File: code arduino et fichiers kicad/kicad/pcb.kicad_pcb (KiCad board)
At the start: 4 copper layers, 53.3 x 101.6 mm, 29 parts, among them U1 LMC6482, U2 LMC6482, U3 LMC6482

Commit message: kasjd
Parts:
- added J1: Screw_Terminal_01x04, Connector_JST:JST_XH_B4B-XH-A_1x04_P2.50mm_Vertical, F.Cu at (85.2, 108.5)
- added J2: Screw_Terminal_01x04, Connector_JST:JST_XH_B4B-XH-A_1x04_P2.50mm_Vertical, F.Cu at (97.7, 108.4)
- added J3: Screw_Terminal_01x02, Connector_JST:JST_XH_B2B-XH-A_1x02_P2.50mm_Vertical, F.Cu at (109.6, 113.5)
- TH1, TH2, TH3: footprint TerminalBlock_Phoenix:TerminalBlock_Phoenix_MPT-0,5-2-2.54_1x02_P2.54mm_Horizontal -> Connector_JST:JST_XH_B2B-XH-A_1x02_P2.50mm_Vertical
- moved R5 28.7 mm to (79.8, 56.2)
- moved R11 27.4 mm to (84.0, 68.3)
- moved R15 26.7 mm to (90.1, 85.4)
- moved R7 20.8 mm to (96.3, 59.2)
- moved R1 20.3 mm to (79.6, 51.5)
- moved R2 20.0 mm to (79.8, 61.2)
- moved U2 16.9 mm to (97.9, 71.7)
- moved R10 16.3 mm to (89.7, 68.1)
- moved U1 15.9 mm to (88.4, 56.9)
- moved TH3 15.7 mm to (116.4, 43.0), turned to 0 degrees
- moved R9 15.2 mm to (89.7, 71.6)
- moved R3 14.6 mm to (96.1, 53.8)
- moved R14 14.5 mm to (84.8, 96.1)
- moved R13 14.3 mm to (90.6, 96.2)
- moved U3 14.2 mm to (98.3, 89.1)
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
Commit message: procrastination pendant optique
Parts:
- removed J3: Screw_Terminal_01x02, Connector_JST:JST_XH_B2B-XH-A_1x02_P2.50mm_Vertical
- added LED1: LED_LEDCHIP-LED0805, LED_SMD:LED_0805_2012Metric_Pad1.15x1.40mm_HandSolder, F.Cu at (78.9, 57.8)
- added R18: 560, Resistor_SMD:R_0805_2012Metric_Pad1.20x1.40mm_HandSolder, F.Cu at (75.1, 57.8)
- moved J1 42.4 mm to (110.0, 74.2)
- moved R11 36.8 mm to (99.1, 101.9), turned to -90 degrees
- moved R12 31.2 mm to (99.1, 106.2), turned to 90 degrees
- moved R7 28.7 mm to (99.3, 87.7), turned to 90 degrees
- moved R6 24.5 mm to (99.3, 83.4), turned to -90 degrees
- moved R8 21.7 mm to (85.0, 83.5), turned to -90 degrees
- moved J2 21.5 mm to (110.2, 91.0)
- moved R10 20.4 mm to (85.0, 87.9), turned to 90 degrees
- moved R15 17.3 mm to (84.9, 101.9), turned to 90 degrees
- moved U3 17.2 mm to (92.0, 105.1)
- moved U2 16.1 mm to (91.9, 86.6)
- moved R4 15.0 mm to (99.3, 68.7), turned to -90 degrees
- moved R1 13.9 mm to (84.9, 64.3), turned to 90 degrees
- moved R5 12.6 mm to (92.1, 59.0), turned to 180 degrees
- moved R13 11.5 mm to (85.0, 106.3), turned to 90 degrees
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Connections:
- power2 pad 4: unconnected-(power2-Pin_4-Pad4) -> +3.3V
- power2 pad 5: unconnected-(power2-Pin_5-Pad5) -> 5V
- power2 pad 7: unconnected-(power2-Pin_7-Pad7) -> GND
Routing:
- net +5V: track 0.00 -> 104.6 mm
- net Net-(U3A--): track 0.00 -> 75.3 mm
- net Net-(U2A--): track 0.00 -> 54.0 mm, vias 0 -> 1
- net T1 sortie: track 0.00 -> 37.3 mm
- net Net-(U1A--): track 0.00 -> 31.7 mm
- net T2 sortie: track 0.00 -> 25.5 mm
- net T3 sortie: track 0.00 -> 18.5 mm
- net Net-(U1B-+): track 0.00 -> 18.3 mm
- net Net-(U2B-+): track 0.00 -> 18.2 mm
- net +3.3V: track 0.00 -> 17.9 mm
- net Net-(U3B-+): track 0.00 -> 17.4 mm
- net pwmgauche: track 0.00 -> 9.46 mm
- net pwmdroite: track 0.00 -> 9.24 mm
- net Net-(U1B--): track 0.00 -> 8.78 mm
- net Net-(U2A-+): track 0.00 -> 8.54 mm
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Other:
- outline, holes or cut-outs redrawn
- board text added: "R14"
- board text added: "analog in"
- board text added: "communication"
- board text added: "digital"
- board text added: "power"
- board text added: "pwm"

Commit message: ksjkasjdh
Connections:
- analogA0-A7 pad 4: unconnected-(analogA0-A7-Pin_4-Pad4) -> /A3
- analogA0-A7 pad 5: unconnected-(analogA0-A7-Pin_5-Pad5) -> /A4
- analogA0-A7 pad 6: unconnected-(analogA0-A7-Pin_6-Pad6) -> /A5
- analogA0-A7 pad 7: unconnected-(analogA0-A7-Pin_7-Pad7) -> /A6
- analogA0-A7 pad 8: unconnected-(analogA0-A7-Pin_8-Pad8) -> /A7
- analogA8-A15 pad 1: unconnected-(analogA8-A15-Pin_1-Pad1) -> /A8
- analogA8-A15 pad 2: unconnected-(analogA8-A15-Pin_2-Pad2) -> /A9
- analogA8-A15 pad 3: unconnected-(analogA8-A15-Pin_3-Pad3) -> /A10
- analogA8-A15 pad 4: unconnected-(analogA8-A15-Pin_4-Pad4) -> /A11
- analogA8-A15 pad 5: unconnected-(analogA8-A15-Pin_5-Pad5) -> /A12
- analogA8-A15 pad 6: unconnected-(analogA8-A15-Pin_6-Pad6) -> /A13
- analogA8-A15 pad 7: unconnected-(analogA8-A15-Pin_7-Pad7) -> /A14
- analogA8-A15 pad 8: unconnected-(analogA8-A15-Pin_8-Pad8) -> /A15
- comm1 pad 1: unconnected-(comm1-Pin_1-Pad1) -> /D14
- comm1 pad 2: unconnected-(comm1-Pin_2-Pad2) -> /D15
- comm1 pad 3: unconnected-(comm1-Pin_3-Pad3) -> /D16
- comm1 pad 4: unconnected-(comm1-Pin_4-Pad4) -> /D17
- comm1 pad 5: unconnected-(comm1-Pin_5-Pad5) -> /D18
- comm1 pad 6: unconnected-(comm1-Pin_6-Pad6) -> /D19
- comm1 pad 7: unconnected-(comm1-Pin_7-Pad7) -> /D20
- comm1 pad 8: unconnected-(comm1-Pin_8-Pad8) -> /D21
- digital1 pad 1: unconnected-(digital1-Pin_1-Pad1) -> +5V
- digital1 pad 18: unconnected-(digital1-Pin_18-Pad18) -> GND
- digital2 pad 1: unconnected-(digital2-Pin_1-Pad1) -> +5V
- digital2 pad 18: unconnected-(digital2-Pin_18-Pad18) -> GND
- power2 pad 2: unconnected-(power2-Pin_2-Pad2) -> +IOREF
- power2 pad 3: unconnected-(power2-Pin_3-Pad3) -> /RESET
- power2 pad 5: 5V -> +5V
- power2 pad 8: unconnected-(power2-Pin_8-Pad8) -> +VIN
- pwm1 pad 1: unconnected-(pwm1-Pin_1-Pad1) -> /D8
- pwm1 pad 10: unconnected-(pwm1-Pin_10-Pad10) -> /SCL
- pwm1 pad 2: unconnected-(pwm1-Pin_2-Pad2) -> /D9
- pwm1 pad 3: unconnected-(pwm1-Pin_3-Pad3) -> /D10
- pwm1 pad 4: unconnected-(pwm1-Pin_4-Pad4) -> pwmgauche
- pwm1 pad 5: unconnected-(pwm1-Pin_5-Pad5) -> /D12
- pwm1 pad 6: unconnected-(pwm1-Pin_6-Pad6) -> /D13
- pwm1 pad 7: pwmgauche -> GND
- pwm1 pad 8: unconnected-(pwm1-Pin_8-Pad8) -> +AREF
- pwm1 pad 9: unconnected-(pwm1-Pin_9-Pad9) -> /SDA
- pwm2 pad 1: unconnected-(pwm2-Pin_1-Pad1) -> /D0/RX0
- pwm2 pad 2: unconnected-(pwm2-Pin_2-Pad2) -> /D1/TX0
- pwm2 pad 3: pwmdroite -> /D2
- pwm2 pad 4: unconnected-(pwm2-Pin_4-Pad4) -> /D3
- pwm2 pad 5: unconnected-(pwm2-Pin_5-Pad5) -> /D4
- pwm2 pad 6: unconnected-(pwm2-Pin_6-Pad6) -> pwmdroite
- pwm2 pad 7: unconnected-(pwm2-Pin_7-Pad7) -> /D6
- pwm2 pad 8: unconnected-(pwm2-Pin_8-Pad8) -> /D7
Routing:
- net +5V: track 104.6 -> 181.4 mm
- net pwmgauche: track 9.46 -> 12.6 mm
- net pwmdroite: track 9.24 -> 12.2 mm

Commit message: pcb yaddi yadda
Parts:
- removed LED1: LED_LEDCHIP-LED0805, LED_SMD:LED_0805_2012Metric_Pad1.15x1.40mm_HandSolder
- added D4: LED, PCM_SparkFun-LED:LED_0603_1608Metric, F.Cu at (79.6, 57.6)
- added TP1: TestPoint, TestPoint:TestPoint_THTPad_D1.5mm_Drill0.7mm, F.Cu at (86.5, 58.8)
- added TP2: TestPoint, TestPoint:TestPoint_THTPad_D1.5mm_Drill0.7mm, F.Cu at (86.0, 78.2)
- added TP3: TestPoint, TestPoint:TestPoint_THTPad_D1.5mm_Drill0.7mm, F.Cu at (86.4, 96.8)
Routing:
- net Net-(U2A--): track 54.0 -> 43.5 mm, vias 1 -> 0
- net +5V: track 181.4 -> 191.1 mm, vias 0 -> 1
- net T2 sortie: track 25.5 -> 33.6 mm
- net Net-(U1A--): track 31.7 -> 25.3 mm
- net T1 sortie: track 37.3 -> 43.5 mm
- net Net-(U3A--): track 75.3 -> 70.0 mm, vias 0 -> 1
- net Net-(D4-A): track 0.00 -> 4.51 mm
- net T3 sortie: track 18.5 -> 22.3 mm
- net (no net): track 2.91 -> 0.00 mm
- net Net-(U3B-+): track 17.4 -> 16.0 mm, vias 0 -> 1
- net Net-(U2A-+): track 8.54 -> 7.17 mm
- net Net-(U1B--): track 8.78 -> 7.48 mm
- net Net-(U3B--): track 5.91 -> 6.76 mm
- net Net-(U1B-+): track 18.3 -> 17.6 mm, vias 0 -> 1
- net Net-(U2B-+): track 18.2 -> 17.8 mm, vias 0 -> 1
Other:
- copper layers 4 -> 2

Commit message: version tht pour pas trop haïr notre vie plus tard
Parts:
- removed J2: Screw_Terminal_01x04, Connector_JST:JST_XH_B4B-XH-A_1x04_P2.50mm_Vertical
- removed R1, R10, R15: 6.1K, Resistor_SMD:R_0805_2012Metric_Pad1.20x1.40mm_HandSolder
- removed digital1, digital2: Conn_01x18_Pin, Connector_PinHeader_2.54mm:PinHeader_1x18_P2.54mm_Vertical
- added C16: 2 μF, Capacitor_THT:CP_Radial_D5.0mm_P2.50mm, F.Cu at (81.9, 59.9)
- added C17: 2 μF, Capacitor_THT:CP_Radial_D5.0mm_P2.50mm, F.Cu at (82.6, 82.8)
- added C18: 2 μF, Capacitor_THT:CP_Radial_D5.0mm_P2.50mm, F.Cu at (82.0, 105.4)
- added J3: Screw_Terminal_01x02, Connector_JST:JST_XH_B2B-XH-A_1x02_P2.50mm_Vertical, F.Cu at (77.0, 45.7)
- added RV1: R_Potentiometer_Trim, Library:trimpot, F.Cu at (76.0, 70.0)
- added RV2: R_Potentiometer_Trim, Library:trimpot, F.Cu at (76.2, 93.0)
- added RV3: R_Potentiometer_Trim, Library:trimpot, F.Cu at (91.2, 117.1)
- D4: footprint PCM_SparkFun-LED:LED_0603_1608Metric -> LED_THT:LED_D5.0mm
- R11, R12, R13, R14, R18, R2, R3, R4, R5, R6, R7, R8, R9: footprint Resistor_SMD:R_0805_2012Metric_Pad1.20x1.40mm_HandSolder -> Resistor_THT:R_Axial_DIN0207_L6.3mm_D2.5mm_P7.62mm_Horizontal
- moved TH3 87.2 mm to (109.2, 132.1), turned to 180 degrees
- moved TH2 86.9 mm to (96.9, 131.8), turned to 180 degrees
- moved TH1 86.6 mm to (85.5, 131.6), turned to 180 degrees
- moved R18 74.6 mm to (77.2, 132.4)
- moved D4 63.6 mm to (77.0, 121.2)
- moved J1 28.4 mm to (108.0, 45.8), turned to 0 degrees
- moved R11 20.4 mm to (106.0, 121.1), turned to 90 degrees
- moved R12 18.9 mm to (110.8, 121.0)
- moved R13 15.2 mm to (89.9, 120.7)
- moved R3 13.4 mm to (112.6, 65.8)
- moved U3 13.3 mm to (97.9, 117.1)
- moved R7 12.9 mm to (112.2, 88.7), turned to -90 degrees
- moved R9 12.1 mm to (102.2, 84.5)
- moved TP3 10.7 mm to (89.6, 107.0)
- moved R5 10.2 mm to (102.1, 60.7)
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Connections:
- J1 pad 3: unconnected-(J1-Pin_3-Pad3) -> pwmdroite
- R18 pad 1: +3.3V -> +5V
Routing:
- net Net-(U1A--): track 25.3 -> 75.1 mm
- net pwmdroite: track 12.2 -> 57.1 mm
- net +5V: track 191.1 -> 162.7 mm, vias 1 -> 0
- net Net-(U3A--): track 70.0 -> 44.3 mm, vias 1 -> 0
- net T3 sortie: track 22.3 -> 46.3 mm
- net Net-(U1A-+): track 6.07 -> 28.2 mm
- net Net-(U2A-+): track 7.17 -> 26.7 mm
- net +3.3V: track 17.9 -> 0.00 mm
- net Net-(U3A-+): track 5.91 -> 23.7 mm
- net pwmgauche: track 12.6 -> 30.1 mm
- net T1 sortie: track 43.5 -> 50.3 mm
- net T2 sortie: track 33.6 -> 39.3 mm
- net Net-(U2A--): track 43.5 -> 48.9 mm
- net Net-(U2B--): track 6.20 -> 10.9 mm
- net Net-(U3B--): track 6.76 -> 11.4 mm
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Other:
- board text removed: "digital"

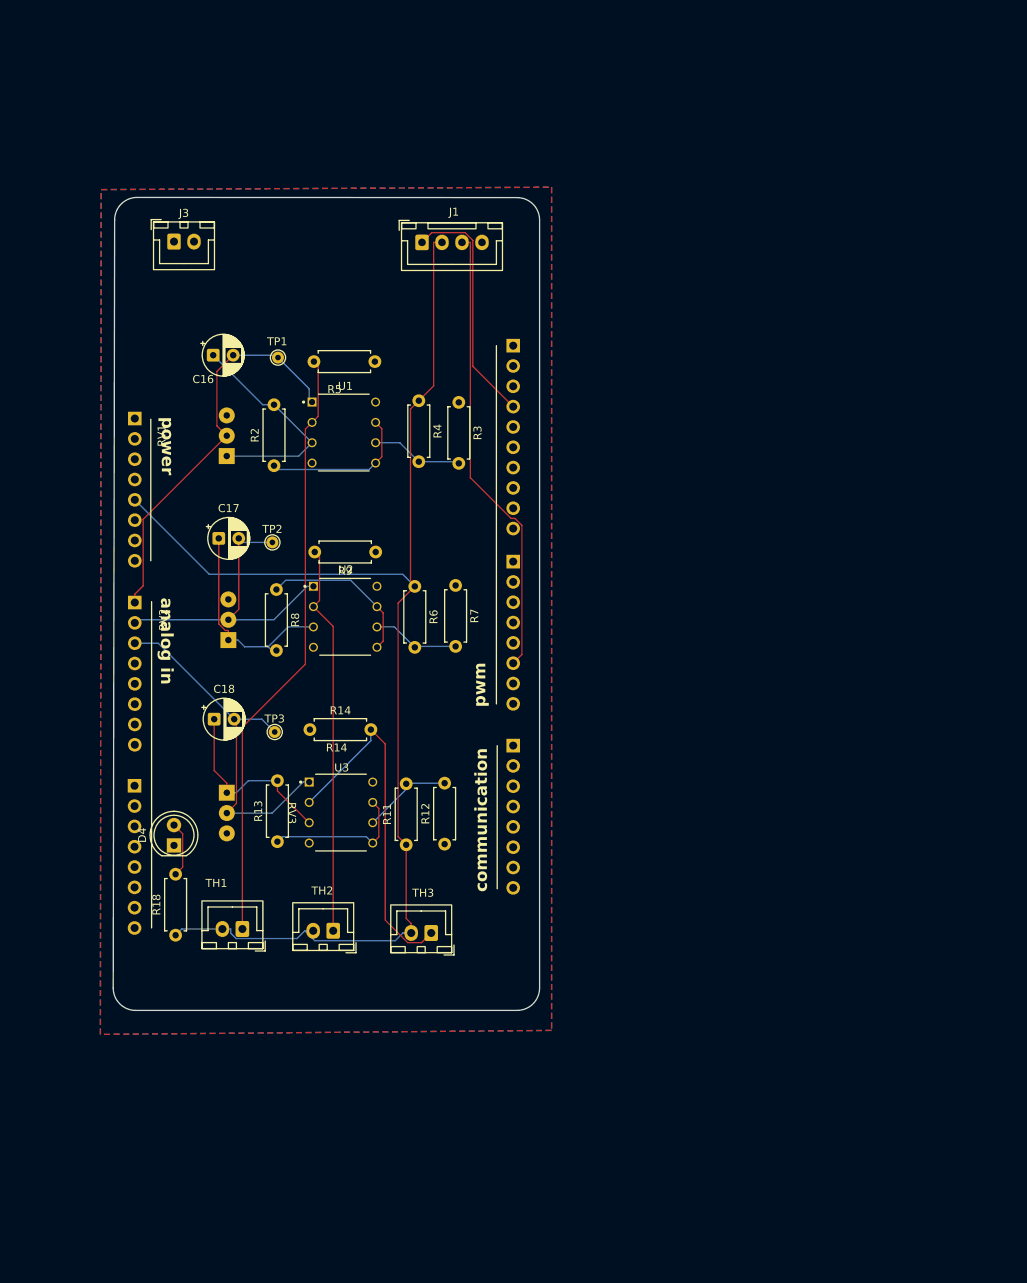
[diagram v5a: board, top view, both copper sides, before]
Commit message: Changment connecteur pcb
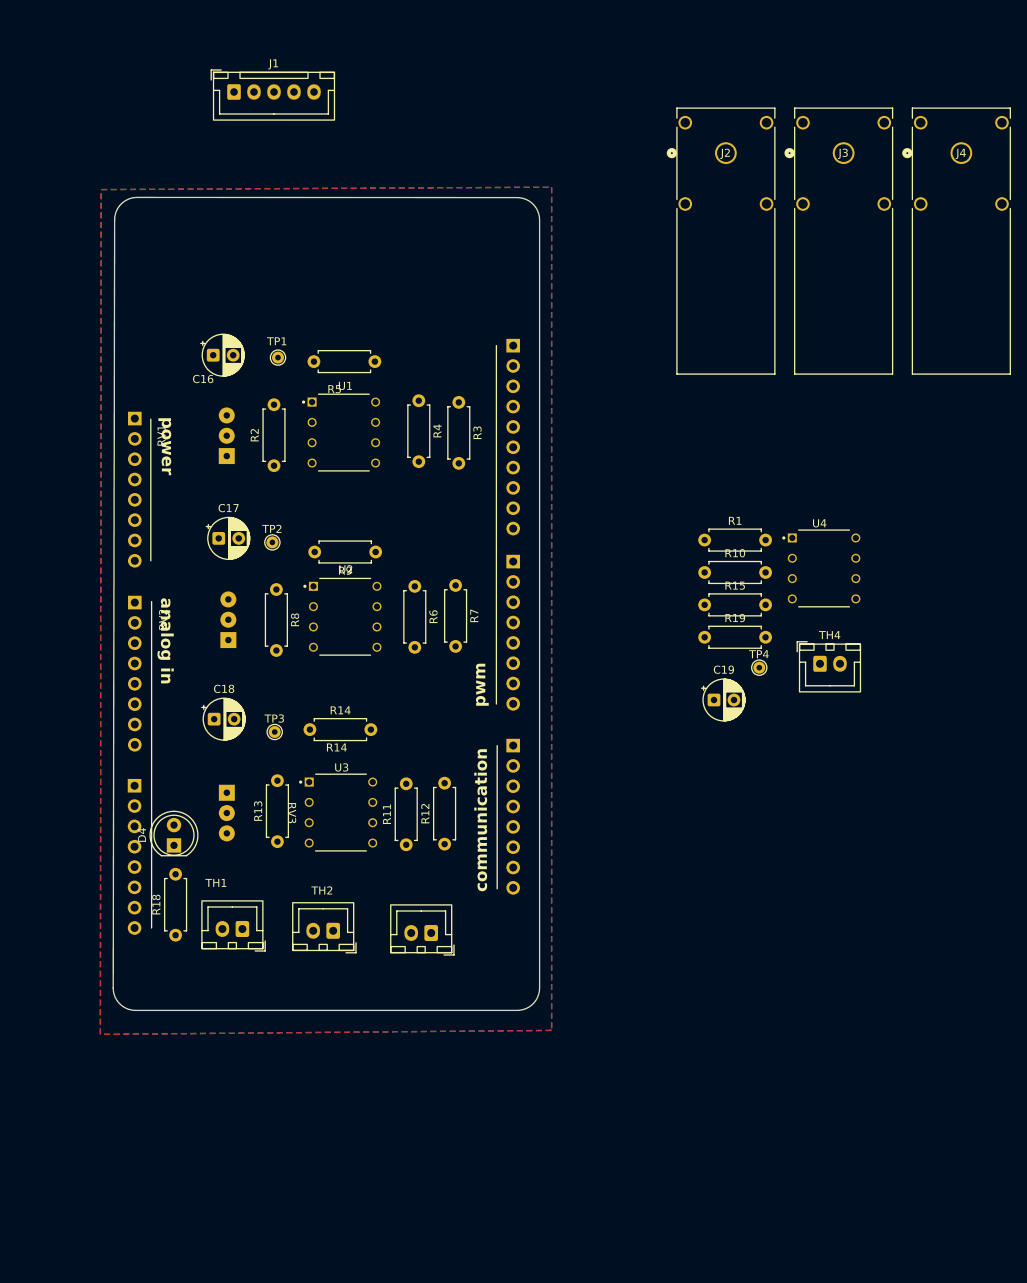
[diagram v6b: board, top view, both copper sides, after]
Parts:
- added C19: 2 μF, Capacitor_THT:CP_Radial_D5.0mm_P2.50mm, F.Cu at (144.5, 103.0)
- added J2: FCR7350R, Connector:CONN1_FCR7350R_CLF, F.Cu at (146.0, 34.6)
- added J4: FCR7350R, Connector:CONN1_FCR7350R_CLF, F.Cu at (175.4, 34.6)
- added R1: 10K, Resistor_THT:R_Axial_DIN0207_L6.3mm_D2.5mm_P7.62mm_Horizontal, F.Cu at (143.3, 83.0)
- added R10: 6.1K, Resistor_THT:R_Axial_DIN0207_L6.3mm_D2.5mm_P7.62mm_Horizontal, F.Cu at (143.3, 87.1)
- added R15: 2K, Resistor_THT:R_Axial_DIN0207_L6.3mm_D2.5mm_P7.62mm_Horizontal, F.Cu at (143.3, 91.1)
- added R19: 6.1K, Resistor_THT:R_Axial_DIN0207_L6.3mm_D2.5mm_P7.62mm_Horizontal, F.Cu at (143.3, 95.2)
- added TH4: Thermistor, Connector_JST:JST_XH_B2B-XH-A_1x02_P2.50mm_Vertical, F.Cu at (157.8, 98.5)
- added TP4: TestPoint, TestPoint:TestPoint_THTPad_D1.5mm_Drill0.7mm, F.Cu at (150.2, 99.0)
- added U4: LMC6482, ampli op:LMC6482, F.Cu at (159.7, 87.8)
- J1: value Screw_Terminal_01x04 -> Screw_Terminal_01x05; footprint Connector_JST:JST_XH_B4B-XH-A_1x04_P2.50mm_Vertical -> Connector_JST:JST_XH_B5B-XH-A_1x05_P2.50mm_Vertical
- J3: value Screw_Terminal_01x02 -> FCR7350R; footprint Connector_JST:JST_XH_B2B-XH-A_1x02_P2.50mm_Vertical -> Connector:CONN1_FCR7350R_CLF
- moved J3 84.4 mm to (160.7, 34.6)
- moved J1 30.1 mm to (84.5, 27.0)
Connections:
- J1 pad 2: +5V -> pwmdroite
- J1 pad 3: pwmdroite -> +8V
- J1 pad 4: GND -> +5V
- J3 pad 1: GND -> +5V
- J3 pad 2: +8V -> (no net)
- analogA0-A7 pad 4: /A3 -> T4 sortie
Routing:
- net +5V: track 162.7 -> 0.00 mm
- net Net-(U1A--): track 75.1 -> 0.75 mm
- net pwmdroite: track 57.1 -> 0.00 mm
- net T1 sortie: track 50.3 -> 0.42 mm
- net Net-(U2A--): track 48.9 -> 0.00 mm
- net T3 sortie: track 46.3 -> 0.40 mm
- net Net-(U3A--): track 44.3 -> 0.00 mm
- net T2 sortie: track 39.3 -> 0.00 mm
- net pwmgauche: track 30.1 -> 0.00 mm
- net Net-(U1A-+): track 28.2 -> 0.01 mm
- net Net-(U2A-+): track 26.7 -> 0.00 mm
- net Net-(U3A-+): track 23.7 -> 0.00 mm
- net Net-(U2B-+): track 20.1 -> 0.00 mm
- net Net-(U1B-+): track 19.0 -> 0.00 mm
- net Net-(U3B-+): track 18.2 -> 0.00 mm
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
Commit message: Pcb quasi fini
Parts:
- added RV4: R_Potentiometer_Trim, Library:trimpot, F.Cu at (102.0, 104.4)
- C16, C17, C18, C19: footprint Capacitor_THT:CP_Radial_D5.0mm_P2.50mm -> Library:condensateur 1uF
- R1, R10, R11, R12, R13, R14, R15, R18, R19, R2, R3, R4, R5, R6, R7, R8, R9: footprint Resistor_THT:R_Axial_DIN0207_L6.3mm_D2.5mm_P7.62mm_Horizontal -> Library:Resistance SMT
- moved J4 92.1 mm to (84.5, 49.5), turned to 180 degrees
- moved R18 71.6 mm to (90.0, 62.0), turned to -90 degrees
- moved U4 66.6 mm to (103.5, 123.5)
- moved J3 63.3 mm to (99.2, 49.5), turned to 180 degrees
- moved D4 60.9 mm to (96.0, 63.3)
- moved TH4 59.4 mm to (112.5, 137.0), turned to 180 degrees
- moved R1 54.1 mm to (111.3, 126.7), turned to 180 degrees
- moved R10 48.6 mm to (111.4, 123.7), turned to 180 degrees
- moved R15 43.6 mm to (111.3, 120.7), turned to 180 degrees
- moved C19 42.0 mm to (102.5, 102.0)
- moved TP4 41.3 mm to (111.0, 112.0)
- moved R19 39.1 mm to (111.3, 117.7), turned to 180 degrees
- moved J2 35.3 mm to (113.9, 49.5), turned to 180 degrees
- moved RV2 34.2 mm to (103.5, 72.4), turned to 0 degrees
- moved R3 32.2 mm to (93.5, 91.7), turned to 180 degrees
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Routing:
- net GND: track 0.00 -> 170.4 mm
- net pwmdroite: track 0.00 -> 97.3 mm
- net Net-(U2A--): track 0.00 -> 95.8 mm
- net Net-(U1A--): track 0.75 -> 76.7 mm
- net T2 sortie: track 0.00 -> 66.5 mm
- net T4 sortie: track 0.00 -> 64.1 mm
- net pwmgauche: track 0.00 -> 59.2 mm
- net +8V: track 0.00 -> 57.9 mm
- net Net-(U1A-+): track 0.01 -> 51.9 mm
- net T3 sortie: track 0.40 -> 50.0 mm
- net Net-(U4A-+): track 0.00 -> 42.9 mm
- net Net-(U2A-+): track 0.00 -> 40.5 mm
- net Net-(U3A--): track 0.00 -> 40.4 mm
- net T1 sortie: track 0.42 -> 39.2 mm
- net Net-(U4A--): track 0.00 -> 37.7 mm
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- added copper zone on F.Cu, net +5V
- removed copper zone on F.Cu, net GND
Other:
- board size 53.3 x 101.6 mm -> 53.5 x 123.1 mm
- board text added: "+5V"
- board text added: "+8V"
- board text added: "GND"
- board text added: "TH3"
- board text added: "pwm G, pwm D,+8V, +5V, GND"
- board text removed: "R14"

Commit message: PCB + BOM
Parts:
- moved pwm1 116.6 mm to (62.3, 160.4), turned to 0 degrees
- moved power2 91.5 mm to (109.6, 151.3), turned to 0 degrees
- moved pwm2 74.4 mm to (62.3, 133.4), turned to 0 degrees
- moved comm1 57.1 mm to (62.3, 110.4), turned to 0 degrees
- moved analogA0-A7 53.0 mm to (109.6, 128.3), turned to 0 degrees
- moved analogA8-A15 38.5 mm to (109.7, 105.4), turned to 0 degrees
- moved R11 30.5 mm to (82.4, 155.6)
- moved R12 30.5 mm to (82.5, 152.6)
- moved R13 30.5 mm to (82.5, 149.6)
- moved R14 30.5 mm to (82.5, 146.6)
- moved C18 30.5 mm to (73.8, 130.9)
- moved C19 30.5 mm to (92.8, 130.9)
- moved RV1 30.5 mm to (74.8, 101.3)
- moved RV2 30.5 mm to (93.8, 101.3)
- moved RV3 30.5 mm to (72.8, 132.8)
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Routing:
- net GND: track 170.4 -> 12.7 mm, vias 0 -> 8
- net pwmdroite: track 97.3 -> 60.5 mm
- net T1 sortie: track 39.2 -> 70.5 mm
- net pwmgauche: track 59.2 -> 89.6 mm
- net Net-(U2A--): track 95.8 -> 65.6 mm, vias 0 -> 1
- net T3 sortie: track 50.0 -> 68.1 mm
- net Net-(U1A-+): track 51.9 -> 34.2 mm, vias 0 -> 1
- net T2 sortie: track 66.5 -> 49.0 mm
- net Net-(U1A--): track 76.7 -> 63.4 mm, vias 0 -> 1
- net +8V: track 57.9 -> 48.8 mm
- net T4 sortie: track 64.1 -> 57.2 mm, vias 0 -> 1
- net Net-(U4A-+): track 42.9 -> 37.0 mm, vias 0 -> 1
- net Net-(U2A-+): track 40.5 -> 35.1 mm, vias 0 -> 1
- net Net-(U4A--): track 37.7 -> 33.5 mm, vias 0 -> 1
- net Net-(U4B-+): track 13.7 -> 17.1 mm
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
